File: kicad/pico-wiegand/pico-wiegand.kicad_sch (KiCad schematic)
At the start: 12 parts, among them Q1 BSS138, U1 Pico

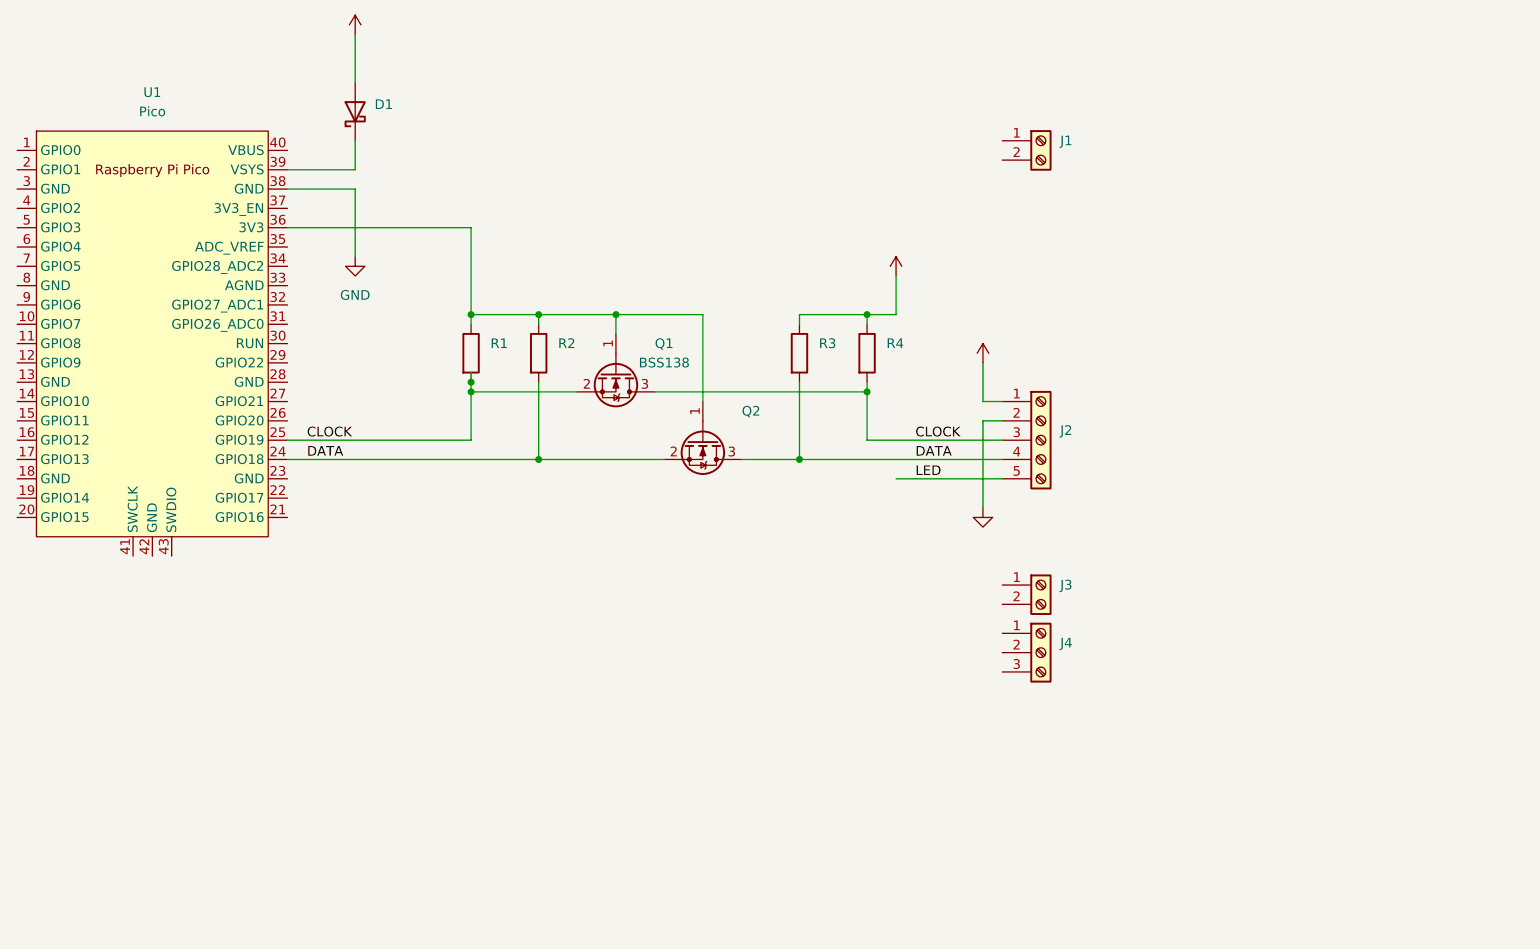
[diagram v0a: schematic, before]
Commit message: Adding LED driver
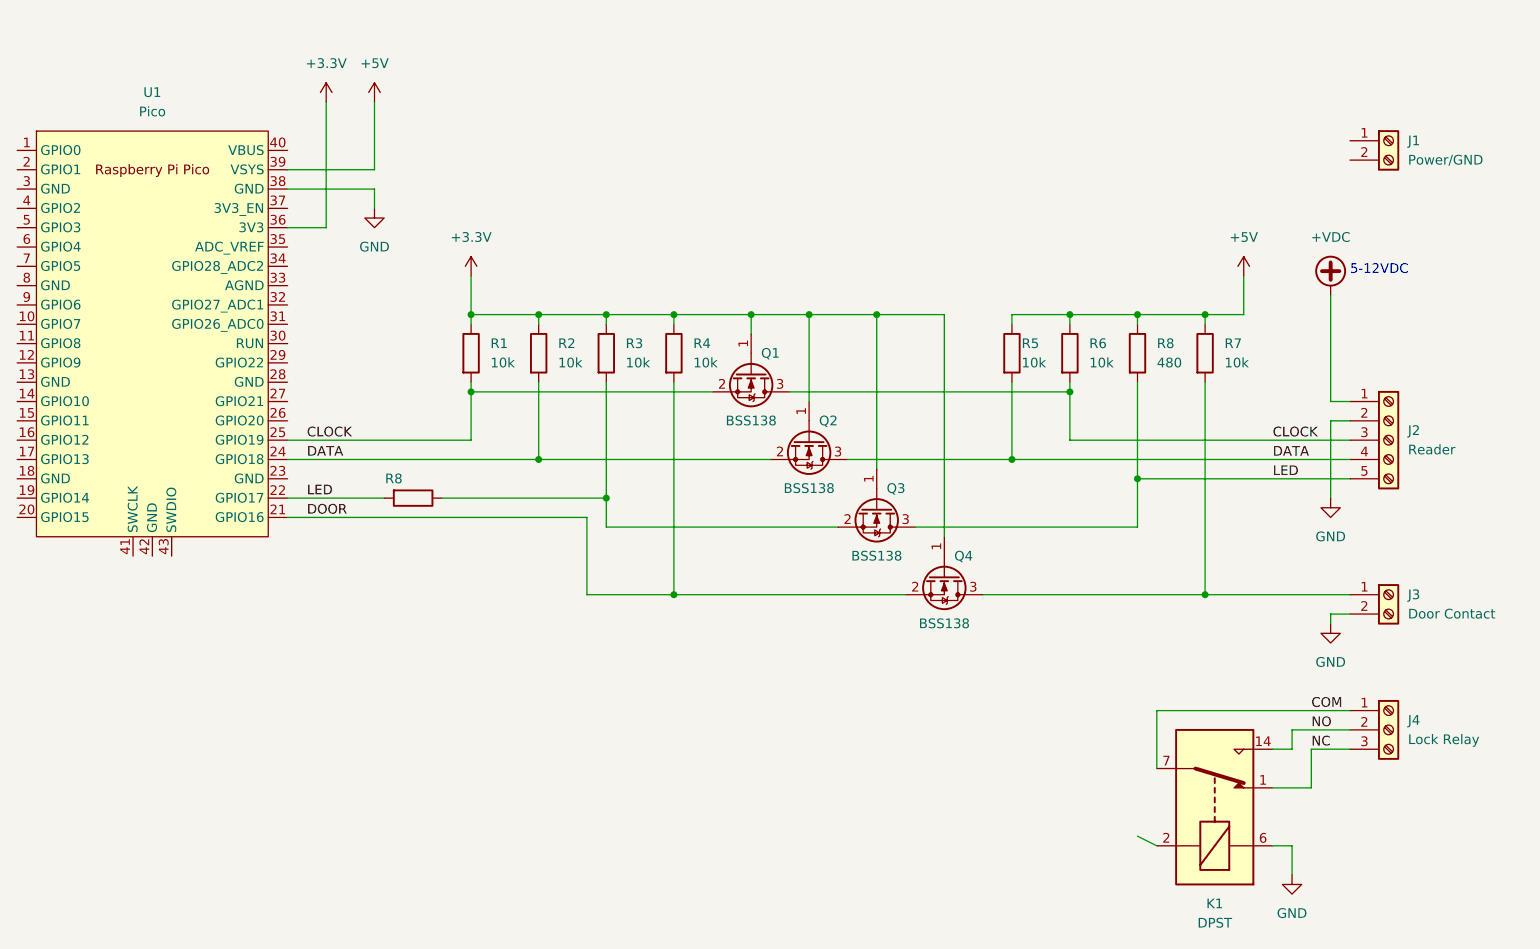
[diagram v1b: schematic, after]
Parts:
- removed D1: (no value), symbol Device:D_Schottky
- added K1: DPST, Relay_THT:Relay_StandexMeder_DIP_LowProfile, symbol Relay:DIPxx-1Cxx-51x
- added Q3, Q4: BSS138, Package_TO_SOT_SMD:SOT-23, symbol Transistor_FET:BSS138
- added R3, R4, R7: 10k, symbol Device:R
- added R8: (no value), symbol Device:R
- added R8: 480, symbol Device:R
- J1: value (none) -> Power/GND
- J2: value (none) -> Reader
- J3: value (none) -> Door Contact
- J4: value (none) -> Lock Relay
- Q2: value (none) -> BSS138; footprint (none) -> Package_TO_SOT_SMD:SOT-23
- R1, R2: value (none) -> 10k
- R5: renamed from R3; value (none) -> 10k
- R6: renamed from R4; value (none) -> 10k
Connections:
- net +5V: now also U1.39 (VSYS), R7.1, R8.1; no longer J2.1 (Pin_1)
- net GND: now also J3.2 (Pin_2), K1.6
- net LED: now also U1.22 (GPIO17), Q3.3 (D), R8.2, R8.2
- net at J3.1 (Pin_1): now also Q4.3 (D), R7.2
- net +3V3: now reaches Q1.1 (G), Q2.1 (G), R1.1, R2.1, U1.36 (3V3)
- net +3V3: now also Q3.1 (G), Q4.1 (G), R3.1, R4.1
- net COM: now reaches J4.1 (Pin_1)
- net COM: now also K1.7, K1.8
- net NO: now reaches J4.2 (Pin_2)
- net NO: now also K1.14
- net NC: now reaches J4.3 (Pin_3)
- net NC: now also K1.1
- net DOOR: now reaches U1.21 (GPIO16)
- net DOOR: now also Q4.2 (S), R4.2
- new net: Q3.2 (S), R3.2, R8.1
- new net +VDC: J2.1 (Pin_1)
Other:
- note added: "5-12VDC"
- company: (none) -> uhppoted
- moved on the sheet: J1, J2, J3, J4, Q1, Q2, R5, R6
